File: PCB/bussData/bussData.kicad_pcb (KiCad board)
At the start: 2 copper layers, 7 parts

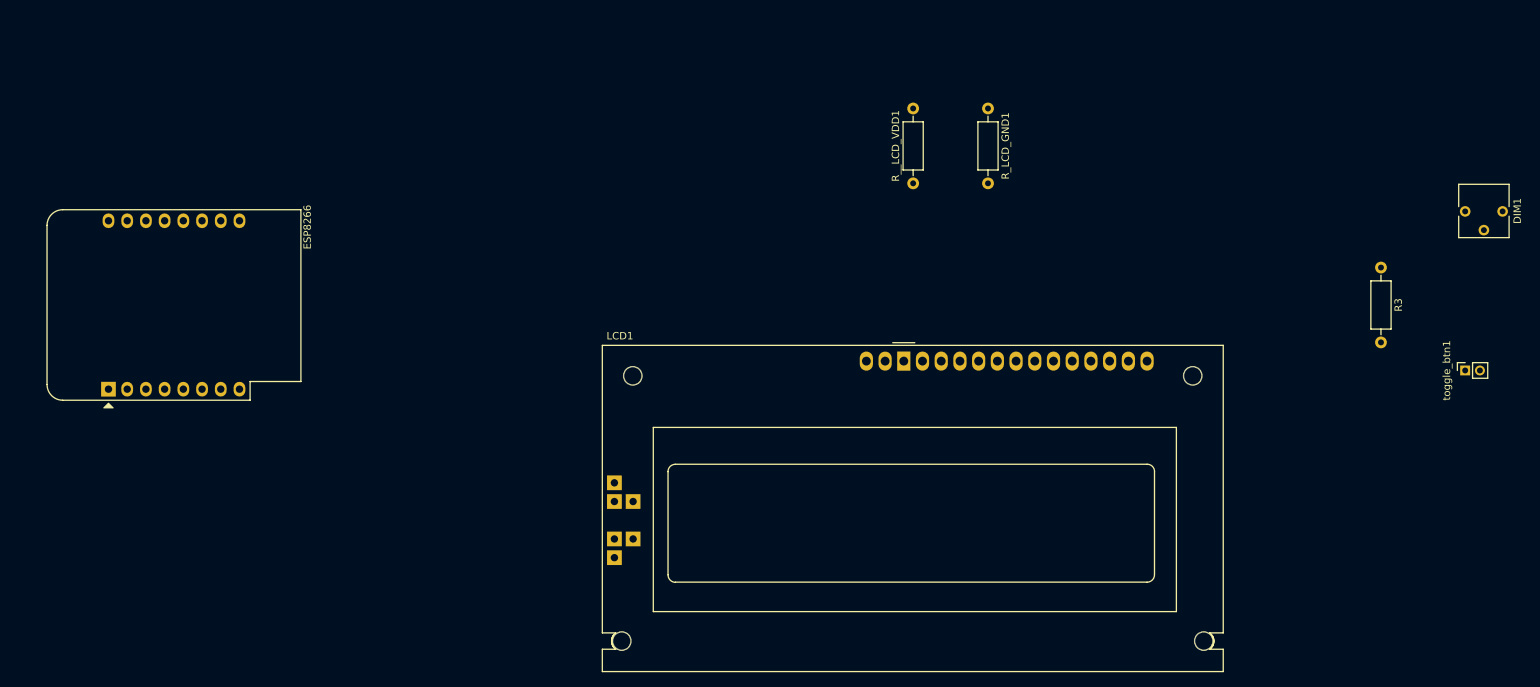
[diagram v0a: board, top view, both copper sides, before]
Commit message: updated the PCB
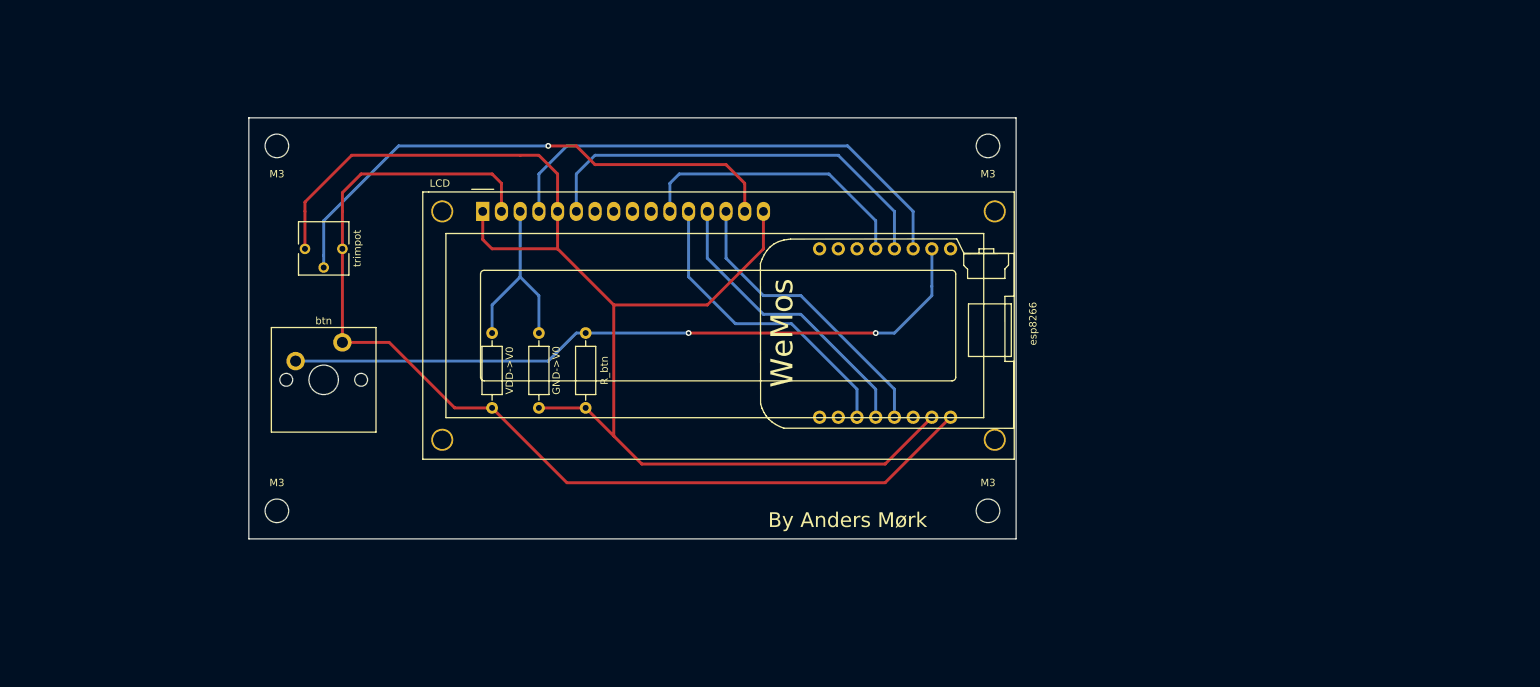
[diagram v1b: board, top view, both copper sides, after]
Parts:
- removed ESP8266: WeMos_D1_mini, Module:WEMOS_D1_mini_light
- removed toggle_btn1: SW_Push_Open, Connector_PinSocket_2.00mm:PinSocket_1x02_P2.00mm_Vertical
- added ?: , , F.Cu at (210.8, 80.0)
- added ?: , , F.Cu at (215.9, 63.5)
- added M3: MountingHole_3.2mm_M3, MountingHole:MountingHole_3.2mm_M3, F.Cu at (209.6, 72.4)
- added M3: MountingHole_3.2mm_M3, MountingHole:MountingHole_3.2mm_M3, F.Cu at (209.6, 121.9)
- added M3: MountingHole_3.2mm_M3, MountingHole:MountingHole_3.2mm_M3, F.Cu at (113.0, 72.4)
- added M3: MountingHole_3.2mm_M3, MountingHole:MountingHole_3.2mm_M3, F.Cu at (113.0, 121.9)
- added btn: SW_Push_Open, Switch_Keyboard_Cherry_MX:SW_Cherry_MX_PCB_1.00u, F.Cu at (119.4, 104.1)
- added esp8266: WeMos_d1_mini, Module:D1_mini_board, F.Cu at (196.8, 97.8)
- LCD: renamed from LCD1; footprint Display:RC1602A -> Display:WC1602A
- moved trimpot 157.6 mm to (116.8, 86.4)
- moved R_btn 109.6 mm to (154.9, 108.0), turned to 90 degrees
- moved GND->V0 68.2 mm to (148.6, 97.8)
- moved LCD 60.7 mm to (141.0, 81.3)
- moved VDD->V0 60.7 mm to (142.2, 97.8), turned to 270 degrees
- renumbered R_LCD_GND1 to GND->V0, R3 to R_btn, R__LCD_VDD1 to VDD->V0, DIM1 to trimpot
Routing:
- net Net-(DIM1-Pad1): track 0.00 -> 185.2 mm
- net Net-(DIM1-Pad3): track 0.00 -> 141.8 mm
- net Net-(R_btn1-Pad2): track 0.00 -> 96.4 mm, vias 0 -> 2
- net Net-(DIM1-Pad2): track 0.00 -> 73.6 mm, vias 0 -> 1
- net Net-(LCD1-Pad4): track 0.00 -> 66.2 mm
- net Net-(LCD1-Pad6): track 0.00 -> 57.5 mm
- net Net-(LCD1-Pad12): track 0.00 -> 41.9 mm
- net Net-(LCD1-Pad13): track 0.00 -> 40.4 mm
- net Net-(LCD1-Pad14): track 0.00 -> 40.4 mm
- net Net-(LCD1-Pad11): track 0.00 -> 38.7 mm
- net Net-(GND1-Pad1): track 0.00 -> 26.8 mm
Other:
- board outline added: 104.1 x 57.2 mm
- board text added: "By Anders Mørk"

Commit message: updated pcb
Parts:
- removed ? (x2): , 
- removed GND->V0, R_btn, VDD->V0: ?, Resistor_THT:R_Axial_DIN0207_L6.3mm_D2.5mm_P10.16mm_Horizontal
- removed LCD: RC1602A, Display:WC1602A
- removed the M3 at (209.6, 72.4)
- removed the M3 at (209.6, 121.9)
- removed the M3 at (113.0, 72.4)
- removed the M3 at (113.0, 121.9)
- removed btn: SW_Push_Open, Switch_Keyboard_Cherry_MX:SW_Cherry_MX_PCB_1.00u
- removed esp8266: WeMos_d1_mini, Module:D1_mini_board
- removed trimpot: R_POT_TRIM, Potentiometer_THT:Potentiometer_Vishay_T73YP_Vertical
- added DIM1: R_POT_TRIM, Potentiometer_THT:Potentiometer_Vishay_T73YP_Vertical, F.Cu at (91.4, 68.6)
- added LCD1: RC1602A, Display:WC1602A, F.Cu at (115.6, 66.0)
- added M3: MountingHole_3.2mm_M3, MountingHole:MountingHole_3.2mm_M3, F.Cu at (184.2, 104.1)
- added REF**: MountingHole_3.2mm_M3, MountingHole:MountingHole_3.2mm_M3, F.Cu at (81.3, 104.1)
- added REF**: MountingHole_3.2mm_M3, MountingHole:MountingHole_3.2mm_M3, F.Cu at (81.3, 58.4)
- added REF**: MountingHole_3.2mm_M3, MountingHole:MountingHole_3.2mm_M3, F.Cu at (184.2, 58.4)
- added R_BTN: ?, Resistor_THT:R_Axial_DIN0207_L6.3mm_D2.5mm_P10.16mm_Horizontal, F.Cu at (85.1, 68.6)
- added R_GND: ?, Resistor_THT:R_Axial_DIN0207_L6.3mm_D2.5mm_P10.16mm_Horizontal, F.Cu at (125.7, 82.5)
- added R_VDD: ?, Resistor_THT:R_Axial_DIN0207_L6.3mm_D2.5mm_P10.16mm_Horizontal, F.Cu at (120.7, 82.5)
- added btn1: SW_Push_Open, Switch_Keyboard_Cherry_MX:SW_Cherry_MX_PCB_1.00u, F.Cu at (94.0, 90.2)
- added esp8266 D1 Wemos mini: WeMos_mini, Module:D1_mini_board, F.Cu at (171.4, 86.4)
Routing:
- net (no net): track 0.00 -> 80.3 mm
- net Net-(DIM1-Pad1): track 185.2 -> 201.1 mm
- net Net-(DIM1-Pad2): track 73.6 -> 61.5 mm, vias 1 -> 0
- net Net-(R_btn1-Pad2): track 96.4 -> 104.1 mm, vias 2 -> 0
- net Net-(DIM1-Pad3): track 141.8 -> 134.9 mm
- net Net-(LCD1-Pad11): track 38.7 -> 41.5 mm
- net Net-(LCD1-Pad14): track 40.4 -> 41.2 mm
- net Net-(LCD1-Pad13): track 40.4 -> 41.2 mm
- net Net-(GND1-Pad1): track 26.8 -> 27.5 mm
- net Net-(LCD1-Pad12): track 41.9 -> 41.2 mm
- added copper zone on B.Cu, net Net-(DIM1-Pad1)
- added copper zone on F.Cu, net Net-(DIM1-Pad3)
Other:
- board size 104.1 x 57.2 mm -> 110.5 x 53.3 mm

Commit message: PCB done
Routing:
- net (no net): track 80.3 -> 36.9 mm
